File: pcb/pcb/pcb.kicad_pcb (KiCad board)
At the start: 2 copper layers, 58.4 x 44.4 mm, 25 parts, among them J1 UART, J2 Barrel_Jack, J3 Stepper, SW1 RESET, SW2 FLASH, U1 ESP32-WROOM-32, U2 TSR_1-2433

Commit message: general tweaks
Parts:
- added REF**: Symbol_Barrel_Polarity, Symbol:Symbol_Barrel_Polarity, F.Cu at (133.2, 64.1)
- H1, H2, H3, H4: footprint MountingHole:MountingHole_3.2mm_M3_DIN965_Pad -> MountingHole:MountingHole_3.2mm_M3_Pad
- REF**: value OSHW-Logo2_7.3x6mm_SilkScreen -> OSHW-Symbol_6.7x6mm_SilkScreen; footprint Symbol:OSHW-Logo2_7.3x6mm_SilkScreen -> Symbol:OSHW-Symbol_6.7x6mm_SilkScreen

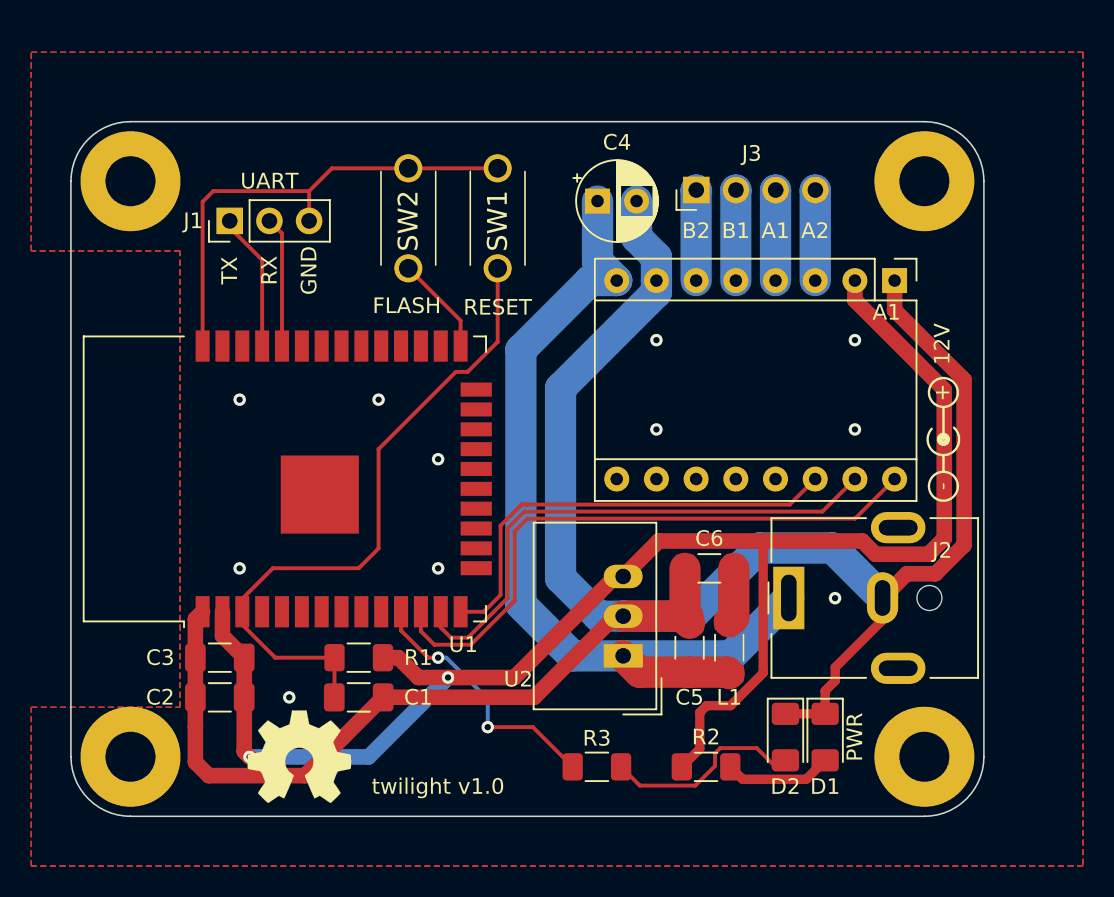
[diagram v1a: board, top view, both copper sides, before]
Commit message: Reroute pcb
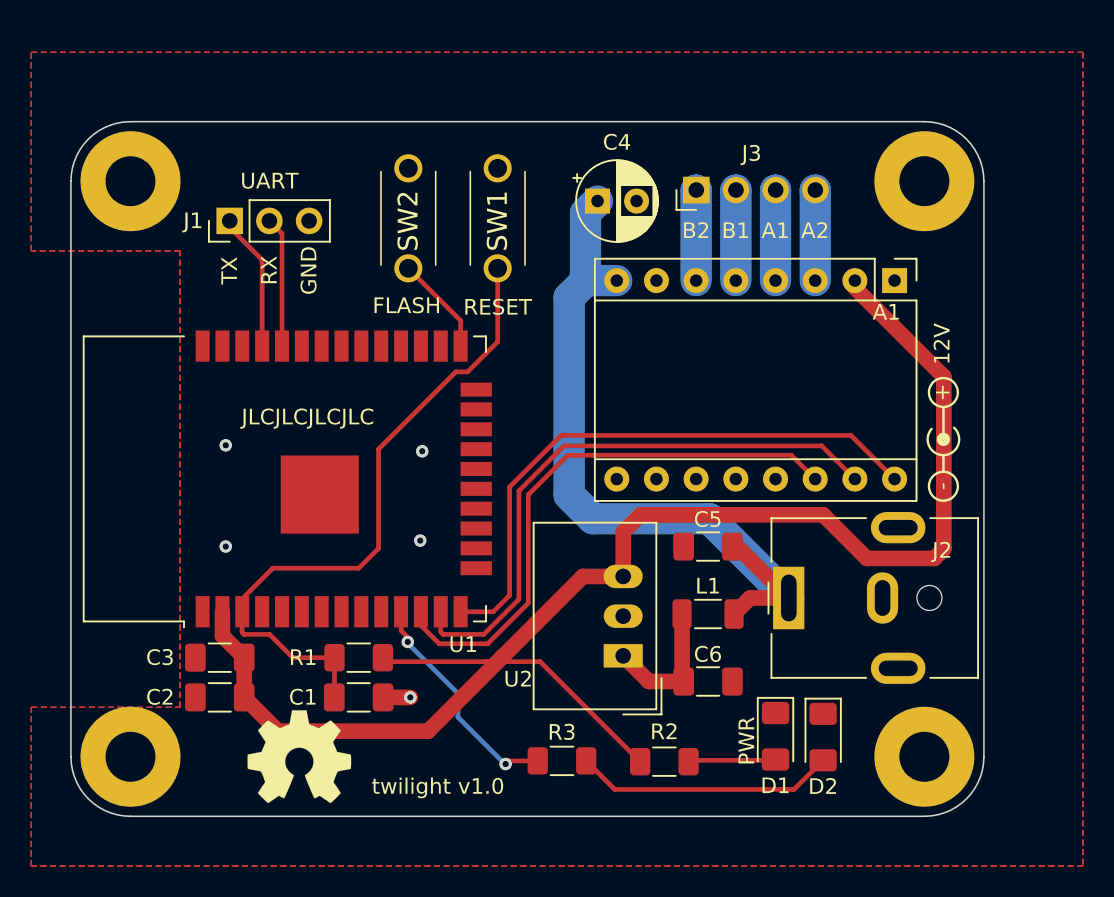
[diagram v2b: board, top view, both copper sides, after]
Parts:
- moved C6 7.24 mm to (118.2, 79.6), turned to 0 degrees
- moved C5 6.58 mm to (118.2, 71.0), turned to 180 degrees
- moved D1 3.18 mm to (122.6, 83.1)
- moved R2 2.69 mm to (115.4, 84.8)
- moved L1 2.55 mm to (118.2, 75.3), turned to 180 degrees
- moved D2 2.41 mm to (125.6, 83.2)
- moved R3 2.27 mm to (108.9, 84.7)
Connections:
- net IO0 renamed /IO0
- U1 pad 12: /DIR -> /SLP
- U1 pad 14: /SLP -> /DIR
- U2 pad 1: +12V -> Net-(C6-Pad1)
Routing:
- net GND: track 169.3 -> 1.74 mm, vias 11 -> 5
- net +12V: track 57.2 -> 47.3 mm
- net /SLP: track 28.8 -> 36.3 mm
- net Net-(C6-Pad1): track 3.54 -> 8.91 mm
- net Net-(D2-Pad2): track 12.4 -> 16.7 mm
- net /STEP: track 34.6 -> 37.8 mm
- net Net-(R3-Pad1): track 16.9 -> 14.7 mm
- net +3V3: track 102.0 -> 99.9 mm, vias 2 -> 0
- net /DIR: track 38.9 -> 37.7 mm
- net Net-(D1-Pad2): track 6.90 -> 5.98 mm
- net /EN: track 42.6 -> 42.0 mm
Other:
- board text added: "JLCJLCJLCJLC"

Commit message: third reddit revision
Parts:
- H1, H3: footprint MountingHole:MountingHole_3.2mm_M3_Pad -> MountingHole:MountingHole_3.2mm_M3
- L1: footprint Inductor_SMD:L_1206_3216Metric_Pad1.22x1.90mm_HandSolder -> Inductor_SMD:L_TracoPower_TCK-141
- moved D2 34.7 mm to (120.9, 48.8)
- moved D1 34.5 mm to (125.5, 48.8)
- moved R3 33.6 mm to (120.9, 53.3)
- moved R2 33.5 mm to (127.0, 53.3), turned to 180 degrees
- moved C4 31.3 mm to (128.1, 75.2)
- moved A1 26.7 mm to (109.5, 70.9), turned to 90 degrees
- moved J3 19.5 mm to (132.3, 60.9), turned to 0 degrees
- moved REF** 15.3 mm to (131.1, 79.2), turned to 0 degrees
- moved SW1 9.91 mm to (114.7, 52.8)
- moved C5 9.60 mm to (110.8, 77.0)
- moved U2 9.57 mm to (104.8, 83.2)
- moved SW2 9.28 mm to (108.3, 52.8)
- moved L1 9.11 mm to (110.8, 80.6)
- moved C6 8.73 mm to (110.7, 84.0)
- moved C1 5.61 mm to (95.4, 75.1)
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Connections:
- J3 pad 1: /B2 -> /A2
- J3 pad 2: /B1 -> /A1
- J3 pad 3: /A1 -> /B1
- J3 pad 4: /A2 -> /B2
- U1 pad 39: GND -> (no net)
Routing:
- net +3V3: track 99.9 -> 62.8 mm
- net +12V: track 47.3 -> 24.9 mm
- net Net-(R3-Pad1): track 14.7 -> 34.7 mm, vias 2 -> 0
- net /DIR: track 37.7 -> 18.2 mm
- net /A2: track 5.80 -> 24.6 mm
- net /A1: track 5.80 -> 20.4 mm
- net /STEP: track 37.8 -> 23.7 mm
- net Net-(D2-Pad2): track 16.7 -> 3.73 mm
- net /B1: track 5.80 -> 16.1 mm
- net /SLP: track 36.3 -> 28.1 mm
- net /EN: track 42.0 -> 49.4 mm
- net /B2: track 5.80 -> 11.8 mm
- net Net-(D1-Pad2): track 5.98 -> 3.10 mm
- net /TX: track 8.45 -> 7.39 mm
- net GND: track 1.74 -> 2.61 mm, vias 5 -> 19
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
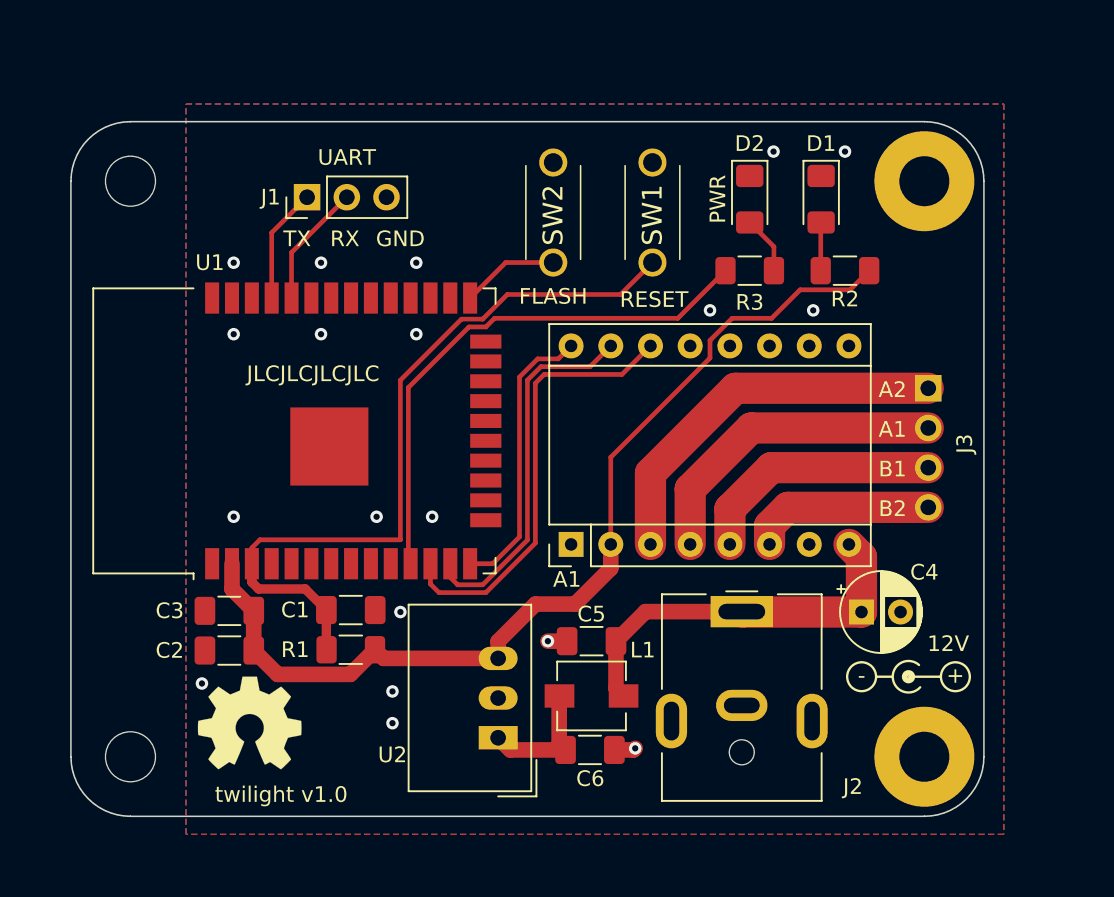
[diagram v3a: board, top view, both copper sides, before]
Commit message: change minimum via size and tweak traces
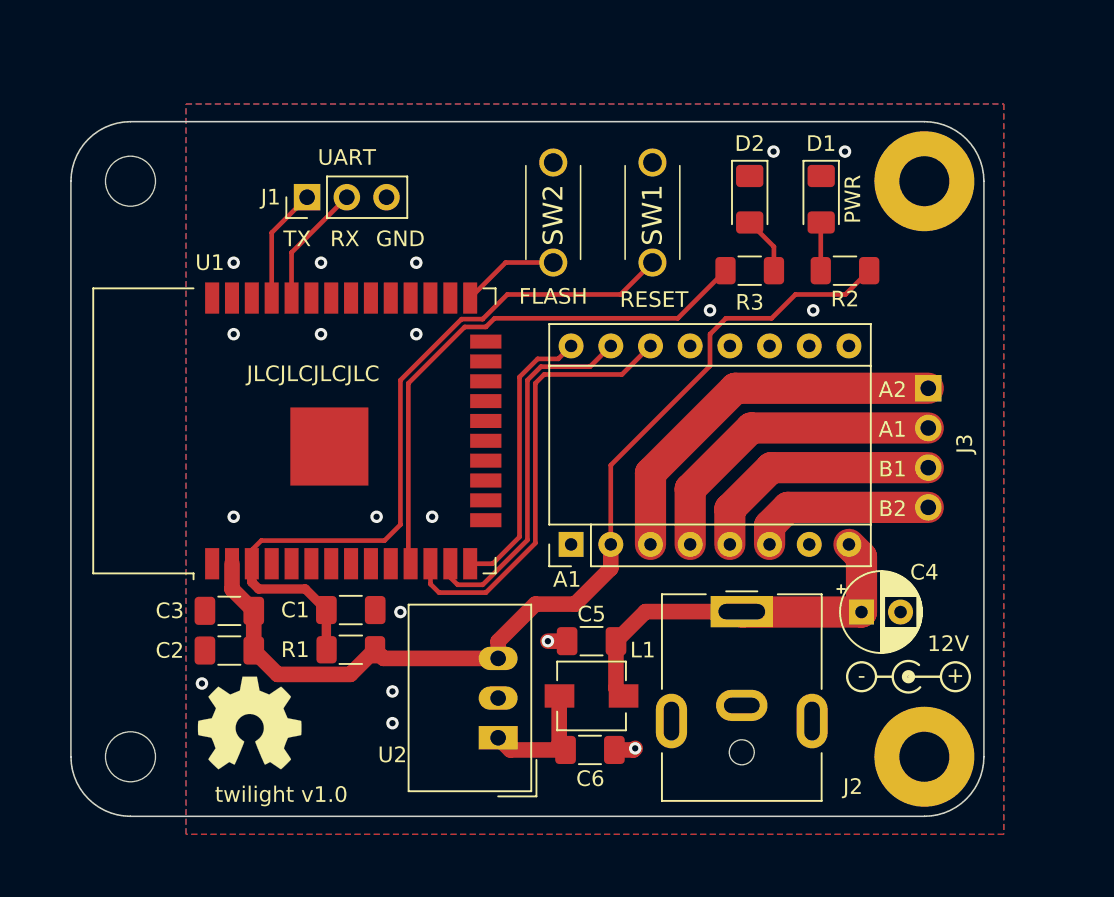
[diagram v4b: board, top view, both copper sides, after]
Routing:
- net /EN: track 49.4 -> 48.8 mm
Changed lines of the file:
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@@
     (effects (font (size 1 1) (thickness 0.15)))
   )
-  (gr_text "PWR" (at 118.872 48.768 90) (layer "F.SilkS")
+  (gr_text "PWR" (at 127.508 48.768 90) (layer "F.SilkS")
     (effects (font (size 1 1) (thickness 0.15)))
   )
@@
   (via (at 118.364 55.88) (size 0.8) (drill 0.4) (layers "F.Cu" "B.Cu") (free) (net 2))
   (via (at 98.552 75.184) (size 0.8) (drill 0.4) (layers "F.Cu" "B.Cu") (free) (net 2))
-  (segment (start 124.130991 54.56452) (end 122.307511 56.388) (width 0.3) (layer "F.Cu") (net 3))
   (segment (start 90.69082 79.17152) (end 89.1671 77.6478) (width 1) (layer "F.Cu") (net 3))
   (segment (start 89.1671 77.6478) (end 89.1671 75.1078) (width 1) (layer "F.Cu") (net 3))
-  (segment (start 118.364 58.928) (end 112.014 65.278) (width 0.3) (layer "F.Cu") (net 3))
   (segment (start 104.8065 77.0575) (end 104.8065 78.1499) (width 1) (layer "F.Cu") (net 3))
   (segment (start 96.927 77.597) (end 97.4799 78.1499) (width 1) (layer "F.Cu") (net 3))
-  (segment (start 118.364 57.800345) (end 118.364 58.928) (width 0.3) (layer "F.Cu") (net 3))
   (segment (start 112.014 72.39) (end 109.728 74.676) (width 1) (layer "F.Cu") (net 3))
-  (segment (start 127.32548 54.56452) (end 124.130991 54.56452) (width 0.3) (layer "F.Cu") (net 3))
-  (segment (start 112.014 65.278) (end 112.014 70.856) (width 0.3) (layer "F.Cu") (net 3))
   (segment (start 112.014 70.856) (end 112.014 72.39) (width 1) (layer "F.Cu") (net 3))
   (segment (start 107.188 74.676) (end 104.8065 77.0575) (width 1) (layer "F.Cu") (net 3))
-  (segment (start 122.307511 56.388) (end 119.776345 56.388) (width 0.3) (layer "F.Cu") (net 3))
+  (segment (start 119.38 56.388) (end 118.364 57.404) (width 0.3) (layer "F.Cu") (net 3))
+  (segment (start 112.014 65.786) (end 112.014 70.856) (width 0.3) (layer "F.Cu") (net 3))
   (segment (start 87.7754 73.7161) (end 87.7754 72.0922) (width 1) (layer "F.Cu") (net 3))
   (segment (start 96.927 77.597) (end 95.35248 79.17152) (width 1) (layer "F.Cu") (net 3))
   (segment (start 97.4799 78.1499) (end 104.8065 78.1499) (width 1) (layer "F.Cu") (net 3))
+  (segment (start 118.364 59.436) (end 112.014 65.786) (width 0.3) (layer "F.Cu") (net 3))
   (segment (start 95.35248 79.17152) (end 90.69082 79.17152) (width 1) (layer "F.Cu") (net 3))
-  (segment (start 128.55 53.34) (end 127.32548 54.56452) (width 0.3) (layer "F.Cu") (net 3))
-  (segment (start 119.776345 56.388) (end 118.364 57.800345) (width 0.3) (layer "F.Cu") (net 3))
+  (segment (start 127.026 54.864) (end 123.831511 54.864) (width 0.3) (layer "F.Cu") (net 3))
+  (segment (start 122.307511 56.388) (end 119.38 56.388) (width 0.3) (layer "F.Cu") (net 3))
+  (segment (start 128.55 53.34) (end 127.026 54.864) (width 0.3) (layer "F.Cu") (net 3))
   (segment (start 109.728 74.676) (end 107.188 74.676) (width 1) (layer "F.Cu") (net 3))
   (segment (start 89.1671 75.1078) (end 87.7754 73.7161) (width 1) (layer "F.Cu") (net 3))
+  (segment (start 118.364 57.404) (end 118.364 59.436) (width 0.3) (layer "F.Cu") (net 3))
+  (segment (start 123.831511 54.864) (end 122.307511 56.388) (width 0.3) (layer "F.Cu") (net 3))
   (segment (start 114.554 70.856) (end 114.554 66.294) (width 2) (layer "F.Cu") (net 6))
   (segment (start 114.554 66.294) (end 119.9821 60.8659) (width 2) (layer "F.Cu") (net 6))
@@
   (segment (start 95.123 48.641) (end 91.5854 52.1786) (width 0.3) (layer "F.Cu") (net 18))
   (segment (start 91.5854 52.1786) (end 91.5854 55.0922) (width 0.3) (layer "F.Cu") (net 18))
-  (segment (start 105.392622 54.864) (end 103.814911 56.441711) (width 0.3) (layer "F.Cu") (net 19))
+  (segment (start 98.552 69.596) (end 97.536 70.612) (width 0.3) (layer "F.Cu") (net 19))
+  (segment (start 102.460689 56.441711) (end 98.552 60.3504) (width 0.3) (layer "F.Cu") (net 19))
   (segment (start 89.0454 73.271222) (end 89.0454 72.0922) (width 0.6) (layer "F.Cu") (net 19))
   (segment (start 93.8145 75.057) (end 93.8145 77.5845) (width 0.6) (layer "F.Cu") (net 19))
+  (segment (start 112.636 54.864) (end 105.392622 54.864) (width 0.3) (layer "F.Cu") (net 19))
+  (segment (start 103.814911 56.441711) (end 102.460689 56.441711) (width 0.3) (layer "F.Cu") (net 19))
   (segment (start 93.8145 77.5845) (end 93.827 77.597) (width 0.6) (layer "F.Cu") (net 19))
-  (segment (start 103.814911 56.441711) (end 102.460689 56.441711) (width 0.3) (layer "F.Cu") (net 19))
   (segment (start 93.8145 75.057) (end 92.46578 73.70828) (width 0.6) (layer "F.Cu") (net 19))
-  (segment (start 98.552 60.3504) (end 98.552 70.5612) (width 0.3) (layer "F.Cu") (net 19))
-  (segment (start 98.552 70.5612) (end 89.5604 70.5612) (width 0.3) (layer "F.Cu") (net 19))
+  (segment (start 114.681 52.819) (end 112.636 54.864) (width 0.3) (layer "F.Cu") (net 19))
+  (segment (start 97.536 70.612) (end 89.646578 70.612) (width 0.3) (layer "F.Cu") (net 19))
   (segment (start 89.482458 73.70828) (end 89.0454 73.271222) (width 0.6) (layer "F.Cu") (net 19))
-  (segment (start 89.0454 71.0762) (end 89.0454 72.0922) (width 0.3) (layer "F.Cu") (net 19))
+  (segment (start 89.646578 70.612) (end 89.0454 71.213178) (width 0.3) (layer "F.Cu") (net 19))
   (segment (start 92.46578 73.70828) (end 89.482458 73.70828) (width 0.6) (layer "F.Cu") (net 19))
-  (segment (start 89.5604 70.5612) (end 89.0454 71.0762) (width 0.3) (layer "F.Cu") (net 19))
-  (segment (start 114.681 52.819) (end 112.636 54.864) (width 0.3) (layer "F.Cu") (net 19))
-  (segment (start 112.636 54.864) (end 105.392622 54.864) (width 0.3) (layer "F.Cu") (net 19))
-  (segment (start 102.460689 56.441711) (end 98.552 60.3504) (width 0.3) (layer "F.Cu") (net 19))
+  (segment (start 105.392622 54.864) (end 103.814911 56.441711) (width 0.3) (layer "F.Cu") (net 19))
+  (segment (start 89.0454 71.213178) (end 89.0454 72.0922) (width 0.3) (layer "F.Cu") (net 19))
+  (segment (start 98.552 60.3504) (end 98.552 69.596) (width 0.3) (layer "F.Cu") (net 19))
   (segment (start 108.331 52.819) (end 105.2886 52.819) (width 0.3) (layer "F.Cu") (net 35))
   (segment (start 105.2886 52.819) (end 103.0154 55.0922) (width 0.3) (layer "F.Cu") (net 35))
-  (segment (start 99.06 60.821789) (end 99.06 71.9468) (width 0.3) (layer "F.Cu") (net 47))
+  (segment (start 104.02182 56.94123) (end 102.667598 56.94123) (width 0.3) (layer "F.Cu") (net 47))
+  (segment (start 119.354 53.34) (end 116.306 56.388) (width 0.3) (layer "F.Cu") (net 47))
+  (segment (start 116.306 56.388) (end 104.57505 56.388) (width 0.3) (layer "F.Cu") (net 47))
   (segment (start 99.06 71.9468) (end 99.2054 72.0922) (width 0.3) (layer "F.Cu") (net 47))
-  (segment (start 119.354 53.34) (end 116.306 56.388) (width 0.3) (layer "F.Cu") (net 47))
-  (segment (start 102.940559 56.94123) (end 99.06 60.821789) (width 0.3) (layer "F.Cu") (net 47))
-  (segment (start 116.306 56.388) (end 104.57505 56.388) (width 0.3) (layer "F.Cu") (net 47))
   (segment (start 104.57505 56.388) (end 104.02182 56.94123) (width 0.3) (layer "F.Cu") (net 47))
-  (segment (start 104.02182 56.94123) (end 102.940559 56.94123) (width 0.3) (layer "F.Cu") (net 47))
+  (segment (start 102.667598 56.94123) (end 99.06 60.548828) (width 0.3) (layer "F.Cu") (net 47))
+  (segment (start 99.06 60.548828) (end 99.06 71.9468) (width 0.3) (layer "F.Cu") (net 47))
   (segment (start 125.45 50.2815) (end 125.476 50.2555) (width 0.3) (layer "F.Cu") (net 48))
   (segment (start 125.45 53.34) (end 125.45 50.2815) (width 0.3) (layer "F.Cu") (net 48))

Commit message: fix mounting hole footprint in schematic
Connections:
- U1 pad 39: (no net) -> GND
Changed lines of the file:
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@@
     (property "Sheetfile" "pcb.kicad_sch")
     (property "Sheetname" "")
-    (attr exclude_from_pos_files exclude_from_bom)
+    (attr exclude_from_pos_files)
     (fp_text reference "H3" (at 0 -4.2) (layer "F.SilkS") hide
       (effects (font (size 1 1) (thickness 0.15)))
@@
       (net 2 "GND") (pinfunction "GND") (pintype "passive"))
     (pad "39" smd rect (at -1 -0.755 90) (size 5 5) (layers "F.Cu" "F.Paste" "F.Mask")
-      (pinfunction "GND") (pintype "passive") (zone_connect 0) (thermal_width 0.1))
+      (net 2 "GND") (pinfunction "GND") (pintype "passive") (zone_connect 0) (thermal_width 0.1))
     (model "${KICAD6_3DMODEL_DIR}/RF_Module.3dshapes/ESP32-WROOM-32.wrl"
       (offset (xyz 0 0 0))
@@
     (property "Sheetfile" "pcb.kicad_sch")
     (property "Sheetname" "")
-    (attr exclude_from_pos_files exclude_from_bom)
+    (attr exclude_from_pos_files)
     (fp_text reference "H1" (at 0 -4.2) (layer "F.SilkS") hide
       (effects (font (size 1 1) (thickness 0.15)))
